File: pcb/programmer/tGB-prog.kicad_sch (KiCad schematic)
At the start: 29 parts, among them J1 USB_B_Micro, J2 PROG_PORT, U1 FT232HL, Y1 FA238V 12MHz

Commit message: update pcb (wip)
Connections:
- net AD2: now also J2.6 (Pin_6); no longer J2.7 (Pin_7)
- net AD3: now also J2.7 (Pin_7); no longer J2.6 (Pin_6)
- net GND: now also D1.1 (A1); no longer D1.2 (A2)
- net USB_DP: now also D1.2 (A2); no longer D1.1 (A1)
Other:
- moved on the sheet: D1
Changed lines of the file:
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@@
+    (stroke (width 0) (type default) (color 0 0 0 0))
+  )
+  (wire (pts (xy 63.5 116.84) (xy 63.5 119.38))
     (stroke (width 0) (type default) (color 0 0 0 0))
   )
@@
     (stroke (width 0) (type default) (color 0 0 0 0))
   )
-  (wire (pts (xy 63.5 116.84) (xy 63.5 119.38))
-    (stroke (width 0) (type default) (color 0 0 0 0))
-  )
   (wire (pts (xy 101.6 115.57) (xy 101.6 116.84))
     (stroke (width 0) (type default) (color 0 0 0 0))
@@
     (effects (font (size 1.27 1.27)) (justify right bottom))
   )
-  (label "AD2" (at 231.14 93.98 180)
+  (label "AD2" (at 231.14 91.44 180)
     (effects (font (size 1.27 1.27)) (justify right bottom))
   )
@@
     (effects (font (size 1.27 1.27)) (justify right bottom))
   )
-  (label "AD3" (at 231.14 91.44 180)
+  (label "AD3" (at 231.14 93.98 180)
     (effects (font (size 1.27 1.27)) (justify right bottom))
   )
@@
     (pin "1")
   )
-  (symbol (lib_id "Device:D_TVS") (at 63.5 107.95 90) (unit 1)
+  (symbol (lib_id "Device:D_TVS") (at 63.5 107.95 270) (unit 1)
     (in_bom yes) (on_board yes) (fields_autoplaced)
     (property "Reference" "D1" (id 0) (at 66.04 106.6799 90)
-      (effects (font (size 1.27 1.27)) (justify right))
+      (effects (font (size 1.27 1.27)) (justify left))
     )
     (property "Value" "DF2S23P2CTC" (id 1) (at 66.04 109.2199 90)
-      (effects (font (size 1.27 1.27)) (justify right))
+      (effects (font (size 1.27 1.27)) (justify left))
     )
     (property "Footprint" "D_SOD-963:D_SOD-963" (id 2) (at 63.5 107.95 0)

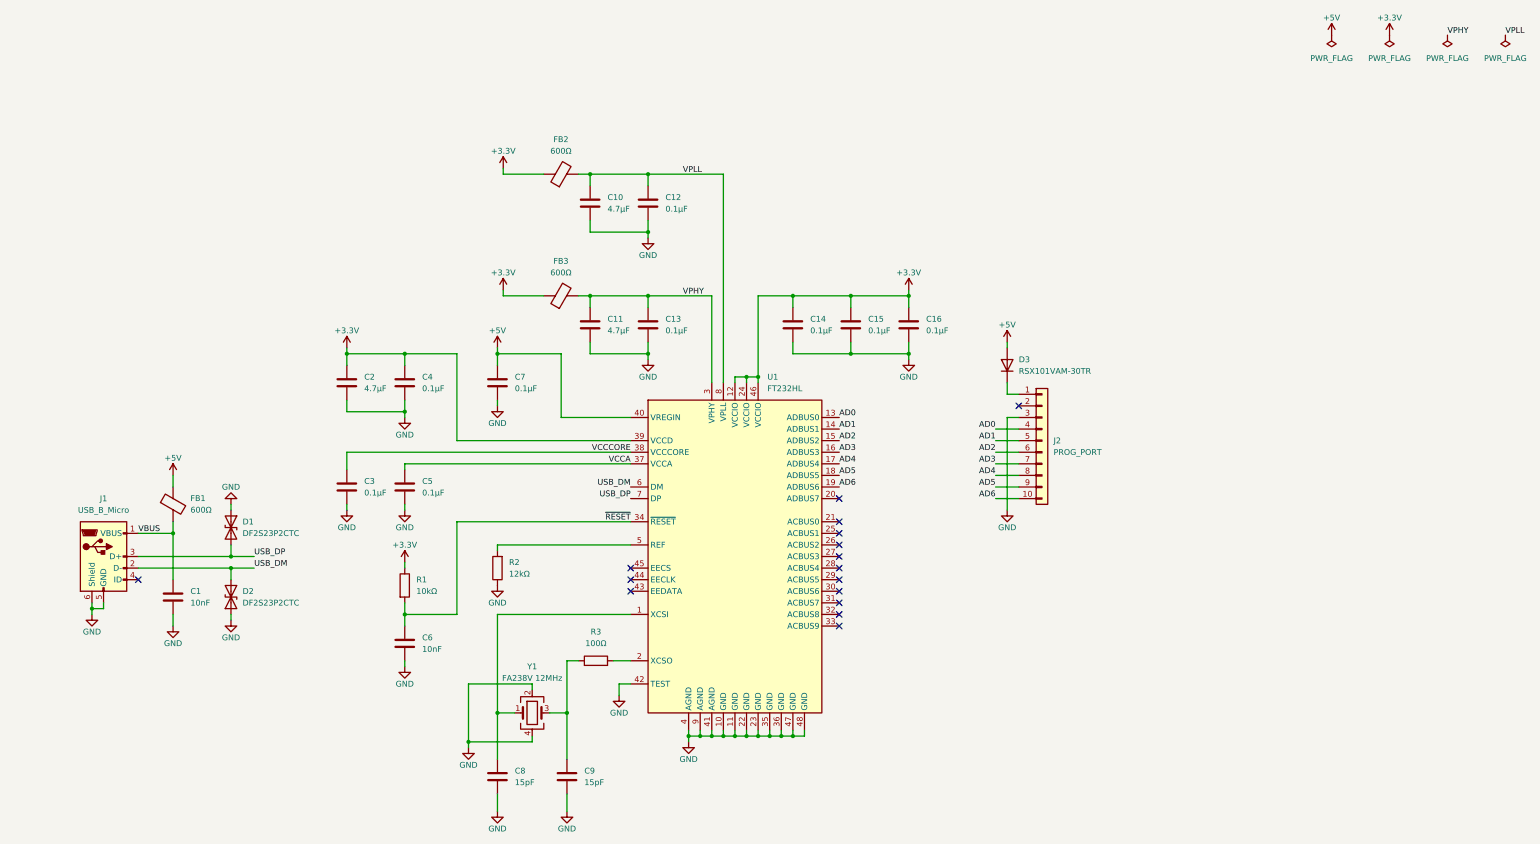
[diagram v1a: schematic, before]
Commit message: replace FT232H with FT2232D to use UART in secondary
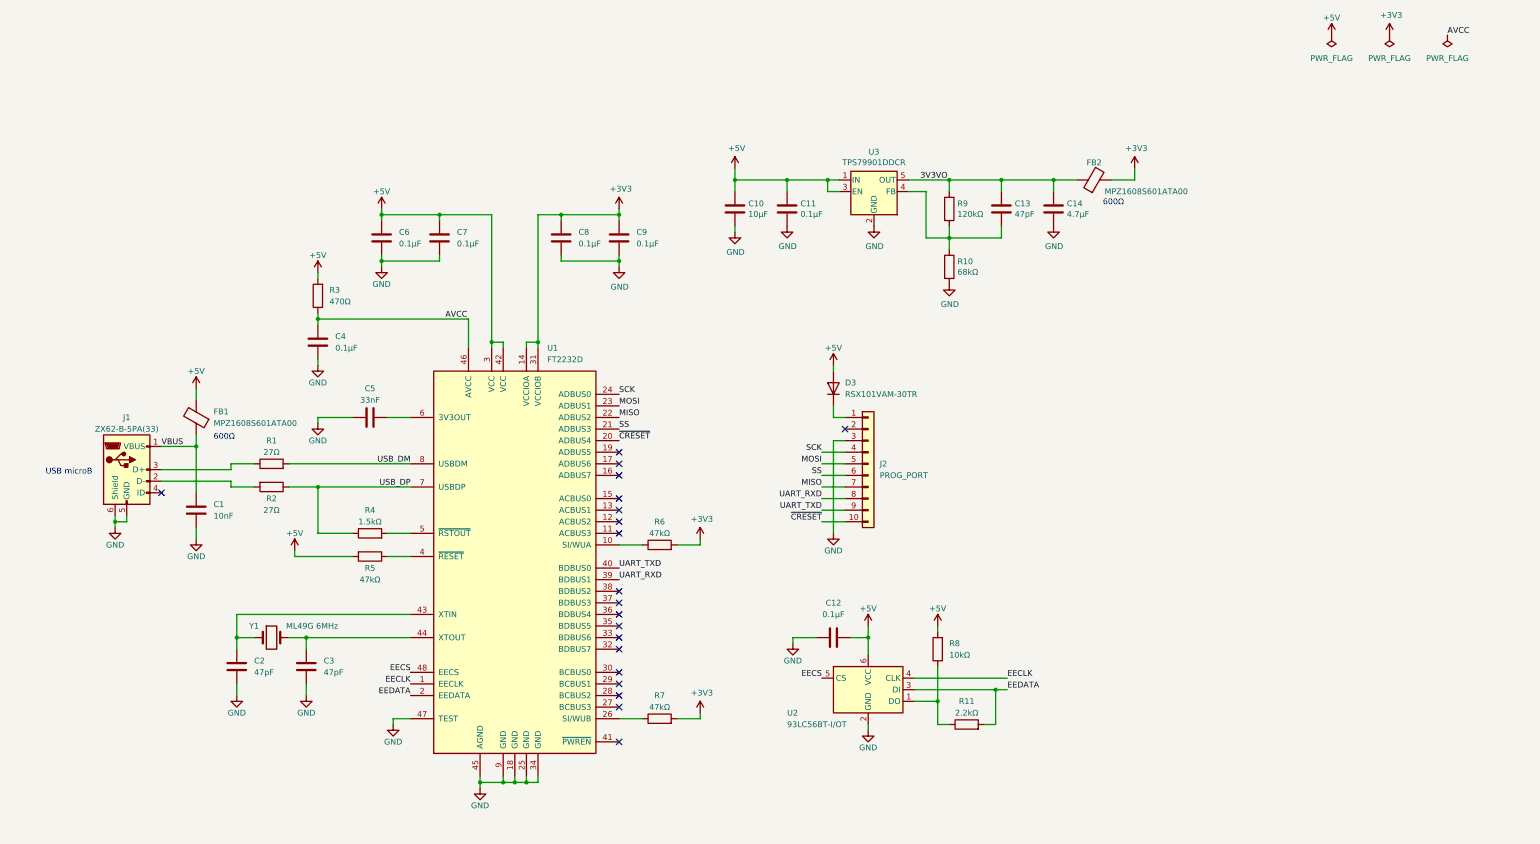
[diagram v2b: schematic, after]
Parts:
- removed C15, C16: 0.1μF, Capacitor_SMD:C_0402_1005Metric, symbol Device:C
- removed D1, D2: DF2S23P2CTC, D_SOD-963:D_SOD-963, symbol Device:D_TVS
- removed FB3: 600Ω, Inductor_SMD:L_0603_1608Metric, symbol Device:FerriteBead
- removed U1: FT232HL, Package_QFP:LQFP-48_7x7mm_P0.5mm, symbol Interface_USB:FT232H
- removed Y1: FA238V 12MHz, Crystal:Crystal_SMD_3225-4Pin_3.2x2.5mm, symbol Device:Crystal_GND24
- added R10: 68kΩ, Resistor_SMD:R_0402_1005Metric, symbol Device:R
- added R11: 2.2kΩ, Resistor_SMD:R_0402_1005Metric, symbol Device:R
- added R4: 1.5kΩ, Resistor_SMD:R_0402_1005Metric, symbol Device:R
- added R5, R6, R7: 47kΩ, Resistor_SMD:R_0402_1005Metric, symbol Device:R
- added R8: 10kΩ, Resistor_SMD:R_0402_1005Metric, symbol Device:R
- added R9: 120kΩ, Resistor_SMD:R_0402_1005Metric, symbol Device:R
- added U1: FT2232D, Package_QFP:LQFP-48_7x7mm_P0.5mm, symbol Interface_USB:FT2232D
- added U2: 93LC56BT-I/OT, Package_TO_SOT_SMD:SOT-23-6, symbol Memory_EEPROM:93LCxxBxxOT
- added U3: TPS79901DDCR, Package_TO_SOT_SMD:SOT-23-5, symbol TPS79901DDCR:TPS79901DDCR
- added Y1: ML49G 6MHz, Crystal:Crystal_SMD_HC49-SD, symbol Device:Crystal
- C10: value 4.7μF -> 10μF; footprint Capacitor_SMD:C_0402_1005Metric -> Capacitor_SMD:C_0603_1608Metric
- C11: value 4.7μF -> 0.1μF
- C13, C3: value 0.1μF -> 47pF
- C14: value 0.1μF -> 4.7μF
- C2: value 4.7μF -> 47pF
- C5: value 0.1μF -> 33nF
- C6: value 10nF -> 0.1μF
- C8, C9: value 15pF -> 0.1μF
- FB1, FB2: value 600Ω -> MPZ1608S601ATA00
- J1: value USB_B_Micro -> ZX62-B-5PA(33)
- R1: value 10kΩ -> 27Ω
- R2: value 12kΩ -> 27Ω
- R3: value 100Ω -> 470Ω
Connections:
- net VCCA is gone; now on net GND: C5.1
- net +5V: now also C10.1, C11.1, C12.2, C6.1, FB1.2, R3.2, R5.2, R8.2, U1.3 (VCC), U1.42 (VCC), U2.6 (VCC), U3.1 (IN), U3.3 (EN); no longer FB1.1
- net GND: now also C12.1, R10.2, U1.18 (GND), U1.25 (GND), U1.34 (GND), U1.45 (AGND), U1.47 (TEST), U1.9 (GND), U2.2 (GND), U3.2 (GND); no longer C12.2, C13.2, C5.2, R2.1
- net USB_DM: now also R1.2, U1.8 (USBDM); no longer J1.2 (D-)
- net USB_DP: now also R2.1, R4.1, U1.7 (USBDP); no longer J1.3 (D+)
- net VBUS: now also FB1.1; no longer FB1.2
- net +3V3: now reaches C9.1
- net +3V3: now also C8.1, FB2.2, R6.2, R7.2, U1.14 (VCCIOA), U1.31 (VCCIOB); no longer R3.1
- net at R2.2: now also J1.2 (D-)
- removed net +3.3V: C14.1, C2.1, C4.1, FB2.1, R1.1
- net AD0 renamed SCK
- net SCK: now also U1.24 (ADBUS0)
- net AD1 renamed MOSI
- net MOSI: now also U1.23 (ADBUS1)
- net AD2 renamed SS
- net SS: now also U1.21 (ADBUS3)
- net AD3 renamed MISO
- net MISO: now also U1.22 (ADBUS2)
- net AD4 renamed UART_RXD
- net UART_RXD: now also U1.39 (BDBUS1)
- net AD5 renamed UART_TXD
- net UART_TXD: now also U1.40 (BDBUS0)
- net AD6 renamed ~{CRESET}
- net ~{CRESET}: now also U1.20 (ADBUS4)
- net VCCCORE: no longer names the net of C3.1
- net VCCCORE: now also U1.44 (XTOUT), Y1.2
- net VPHY renamed 3V3VO
- net 3V3VO: now also C14.1, FB2.1, R9.1, U3.5 (OUT); no longer C11.1
- removed net VPLL: C10.1, C12.1, FB2.2
- removed net ~{RESET}: C6.1, R1.2
- new net: R4.2, U1.5 (~{RSTOUT})
- new net: R11.1, R8.1, U2.1 (DO)
- new net: R5.1, U1.4 (~{RESET})
- new net: C13.2, R10.1, R9.2, U3.4 (FB)
- new net: C2.1, U1.43 (XTIN), Y1.1
- new net: C5.2, U1.6 (3V3OUT)
- new net: R6.1, U1.10 (SI/WUA)
- new net: R7.1, U1.26 (SI/WUB)
- new net: J1.3 (D+), R1.1
- new net AVCC: C4.1, R3.1, U1.46 (AVCC)
- new net EECLK: U1.1 (EECLK), U2.4 (CLK)
- new net EECS: U1.48 (EECS), U2.5 (CS)
- new net EEDATA: R11.2, U1.2 (EEDATA), U2.3 (DI)
- no-connect marks 16 -> 20
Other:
- note added: "600Ω"
- note added: "USB microB"
- moved on the sheet: C1, D3, J1, J2

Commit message: complete placement and route of components, DRC passed with warnings
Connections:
- net +5V_GB: now reaches D3.1 (K), J2.1 (Pin_1)
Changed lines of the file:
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@@
     (effects (font (size 1.27 1.27)) (justify left bottom))
+  )
+  (label "+5V_GB" (at 195.58 83.82 180)
+    (effects (font (size 1.27 1.27)) (justify right bottom))
   )
   (label "MISO" (at 148.59 83.82 0)

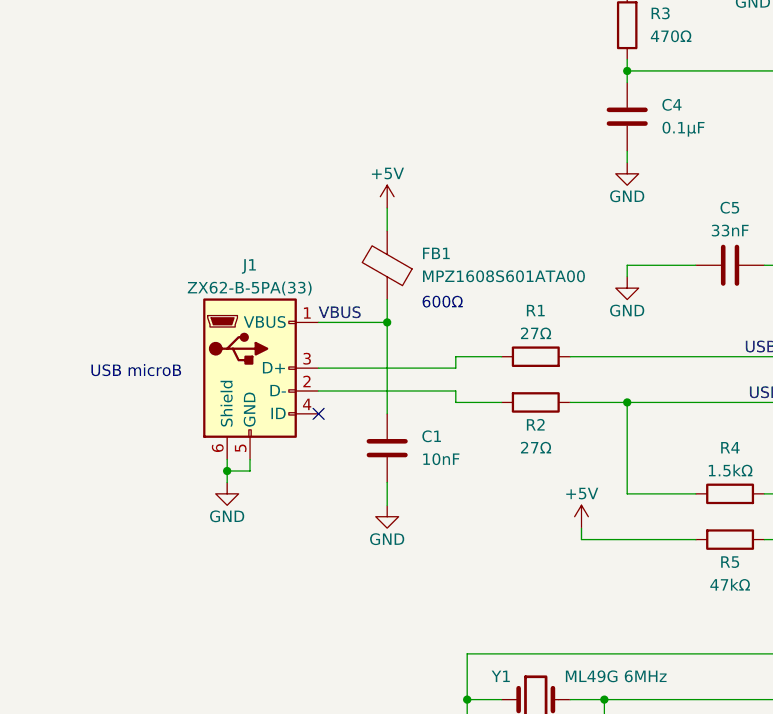
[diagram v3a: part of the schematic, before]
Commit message: fix D+ and D- polarity reversal on USB
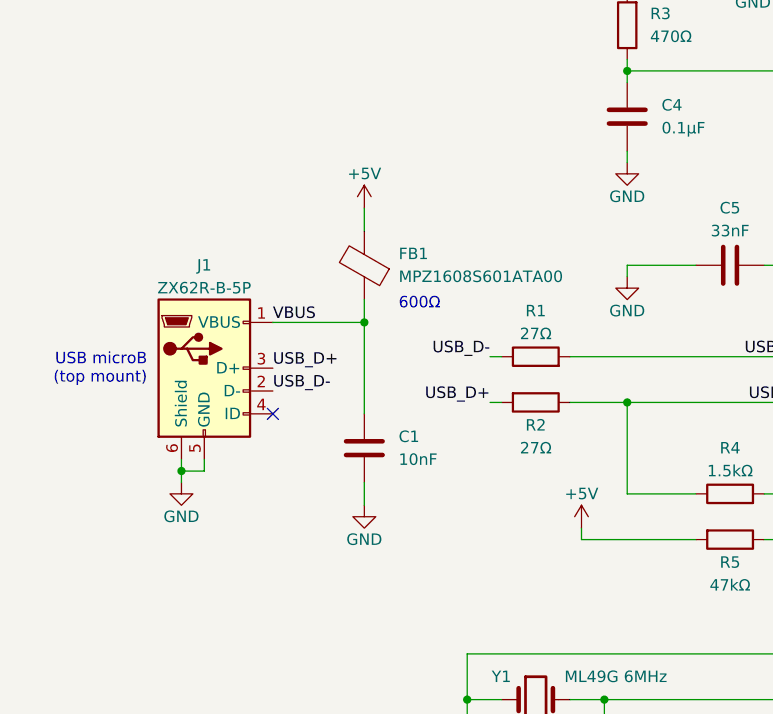
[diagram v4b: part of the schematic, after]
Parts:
- J1: value ZX62-B-5PA(33) -> ZX62R-B-5P; footprint ZX62-B-5PA:ZX62-B-5PA(33) -> ZX62R-B-5P:ZX62R-B-5P
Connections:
- net USB_D+: now reaches J1.3 (D+)
- net USB_D+: now also R2.2; no longer R1.1
- net USB_D-: now reaches J1.2 (D-)
- net USB_D-: now also R1.1; no longer R2.2
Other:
- note added: "USB microB (top mount)"
- note removed: "USB microB"
- moved on the sheet: C1, FB1, J1

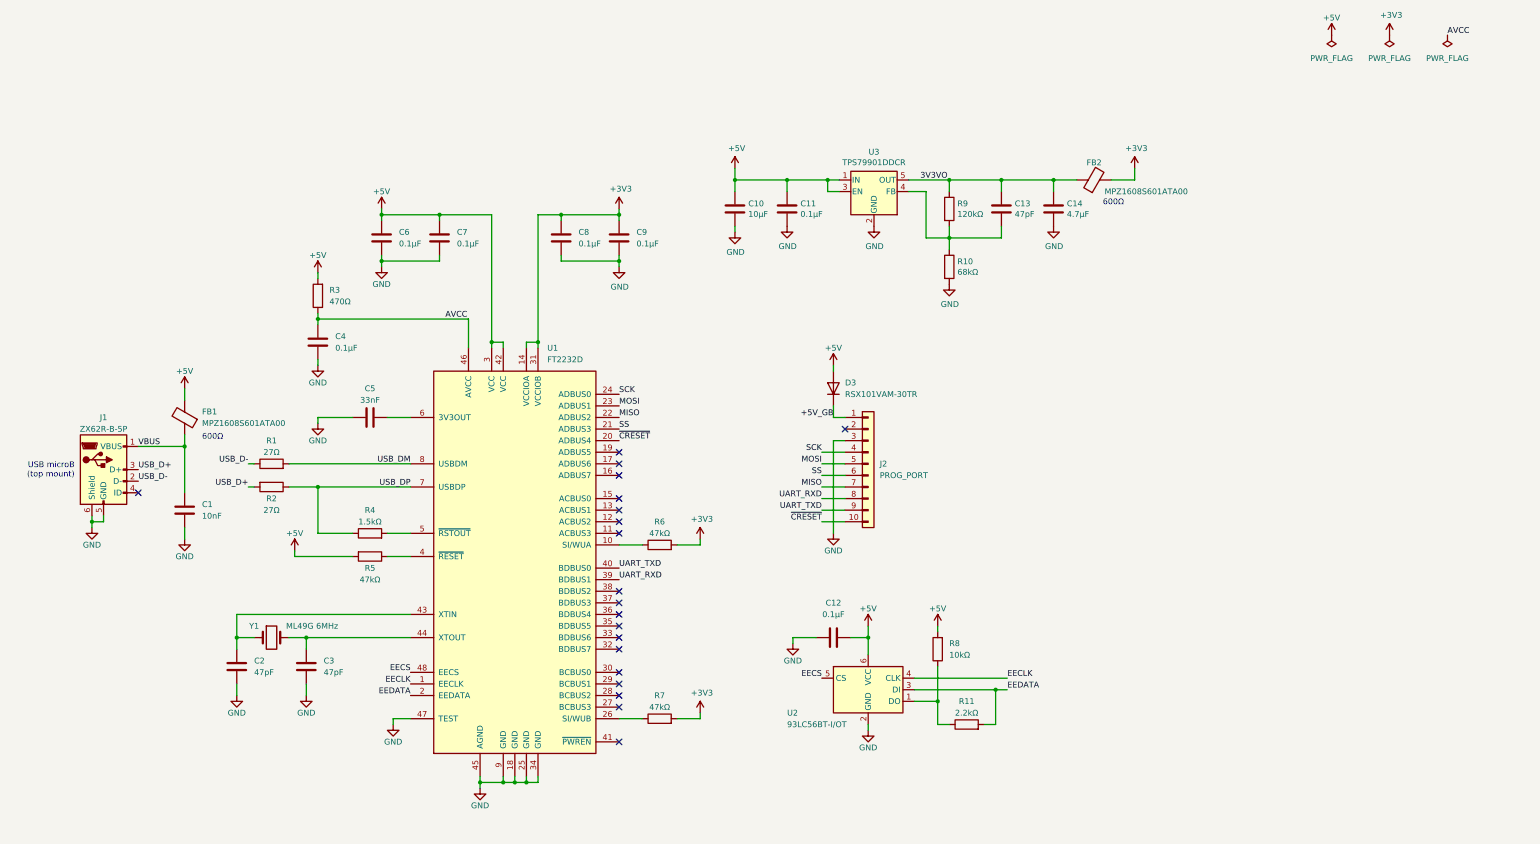
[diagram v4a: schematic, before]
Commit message: change Y1 parts, centering of USB connector
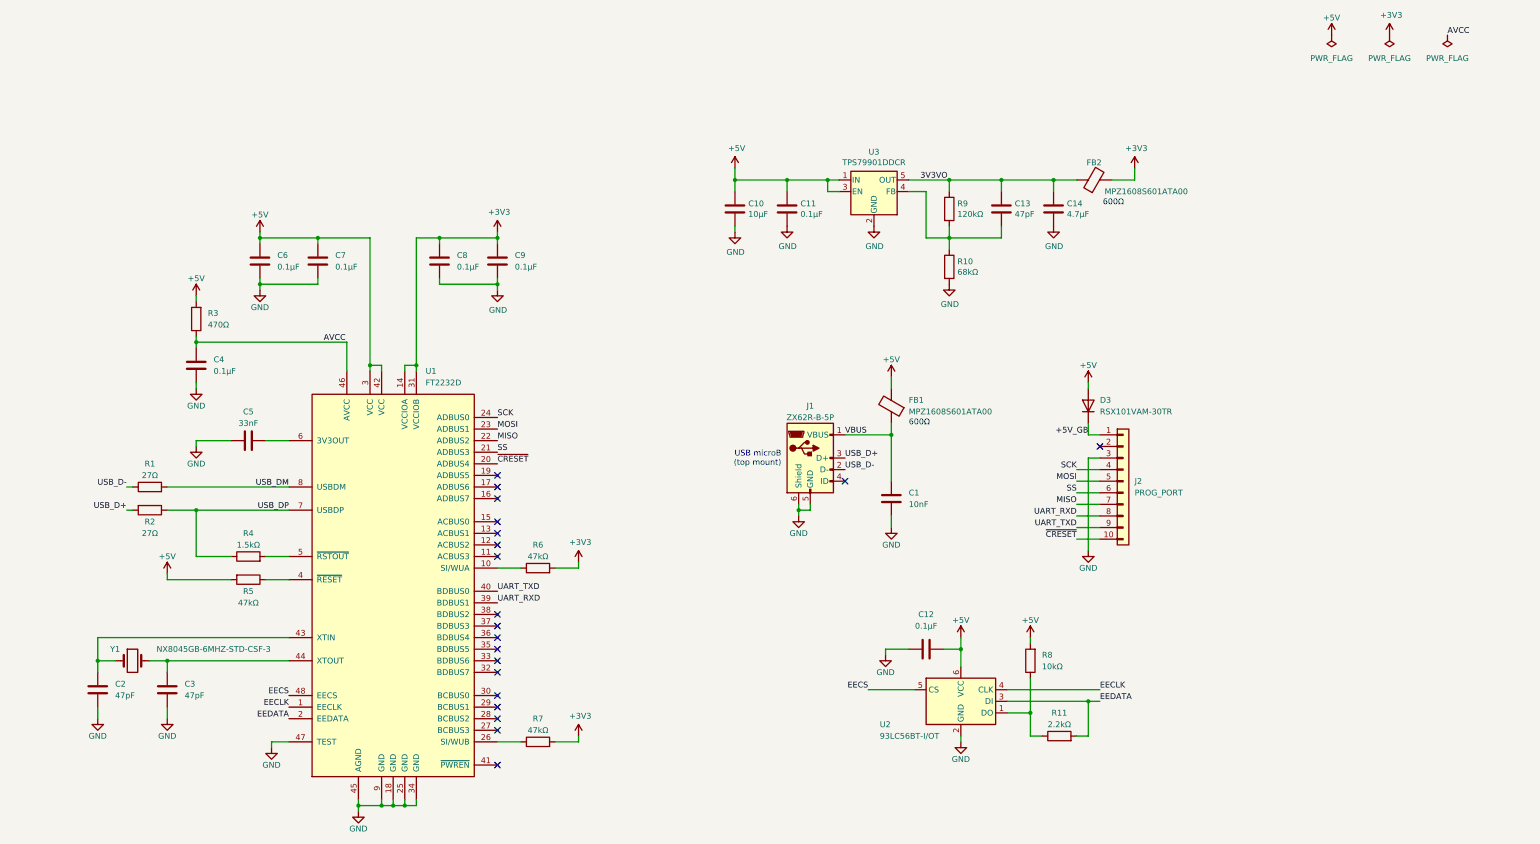
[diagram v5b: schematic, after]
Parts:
- Y1: value ML49G 6MHz -> NX8045GB-6MHZ-STD-CSF-3; footprint Crystal:Crystal_SMD_HC49-SD -> Crystal:Crystal_SMD_TXC_AX_8045-2Pin_8.0x4.5mm
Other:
- moved on the sheet: C1, C12, C2, C3, C4, C5, C6, C7, C8, C9, D3, FB1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
